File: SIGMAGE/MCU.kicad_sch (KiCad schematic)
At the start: 22 parts, among them U8 STM32F407VGTx, X1 STDCSU18M

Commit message: Finished schematic
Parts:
- added J10, J9: TSW10607GS, SIGMAGE:TSW10607GS, symbol SIGMAGE:TSW10607GS
- added J11, J12, J13: HTSW10807GD, SIGMAGE:HTSW10807GD, symbol SIGMAGE:HTSW10807GD
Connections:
- net ADC1_BYPAS: now also U8.93 (PB7)
- net ADC1_PDWN: now also U8.92 (PB6)
- net ADC2_BYPAS: now also U8.96 (PB9)
- net ADC2_DOUT: now also U8.91 (PB5); no longer U8.80 (PC12)
- net ADC2_LRCK: now also U8.29 (PA4); no longer U8.77 (PA15)
- net ADC2_PDWN: now also U8.95 (PB8)
- net GND: now also J10.6, J9.6
- net at U8.1 (PE2): now also J11.3
- net at U8.15 (PC0): now also J13.9
- net PHY_MDC: now reaches U8.16 (PC1)
- net at U8.17 (PC2): now also J13.10
- net at U8.18 (PC3): now also J13.11
- net at U8.2 (PE3): now also J11.4
- net at U8.23 (PA0): now also J13.1
- net PHY_REFCLK: now reaches U8.24 (PA1)
- net PHY_MDIO: now reaches U8.25 (PA2)
- net at U8.26 (PA3): now also J13.2
- net at U8.3 (PE4): now also J11.5
- net at U8.30 (PA5): now also J13.3
- net at U8.31 (PA6): now also J13.4
- net PHY_CRS_DV: now reaches U8.32 (PA7)
- net PHY_RXD0: now reaches U8.33 (PC4)
- net PHY_RXD1: now reaches U8.34 (PC5)
- net at U8.35 (PB0): now also J13.5
- net at U8.36 (PB1): now also J13.6
- net at U8.37 (PB2): now also J13.7
- net at U8.38 (PE7): now also J11.8
- net at U8.39 (PE8): now also J11.9
- net at U8.4 (PE5): now also J11.6
- net at U8.40 (PE9): now also J11.10
- net at U8.41 (PE10): now also J11.11
- net at U8.42 (PE11): now also J11.12
- net at U8.43 (PE12): now also J11.13
- net at U8.44 (PE13): now also J11.14
- net at U8.45 (PE14): now also J11.15
- net at U8.46 (PE15): now also J11.16
- net PHY_NRST: now reaches U8.47 (PB10)
- net PHY_TXEN: now reaches U8.48 (PB11)
- net at U8.5 (PE6): now also J11.7
- net at U8.53 (PB14): now also J13.8
- net at U8.55 (PD8): now also J12.9
- net at U8.56 (PD9): now also J12.10
- net at U8.57 (PD10): now also J12.11
- net at U8.58 (PD11): now also J12.12
- net at U8.59 (PD12): now also J12.13
- net at U8.60 (PD13): now also J12.14
- net at U8.61 (PD14): now also J12.15
- net at U8.62 (PD15): now also J12.16
- net at U8.65 (PC8): now also J13.12
- net at U8.66 (PC9): now also J13.13
- net USART1_CK: now reaches U8.67 (PA8)
- net USART1_CK: now also J9.5
- net USART1_TX: now reaches U8.68 (PA9)
- net USART1_TX: now also J9.3
- net USART1_RX: now reaches U8.69 (PA10)
- net USART1_RX: now also J9.4
- net PHY_TXD1: now reaches U8.7 (PC13)
- net USART1_CTS: now reaches U8.70 (PA11)
- net USART1_CTS: now also J9.1
- net USART1_RTS: now reaches U8.71 (PA12)
- net USART1_RTS: now also J9.2
- net JTMS_SWDIO: now reaches U8.72 (PA13)
- net JTMS_SWDIO: now also J10.1
- net JTCK_SWCLK: now reaches U8.76 (PA14)
- net JTCK_SWCLK: now also J10.2
- net at U8.79 (PC11): now also J13.14
- net at U8.8 (PC14): now also J13.15
- net at U8.81 (PD0): now also J12.1
- net at U8.82 (PD1): now also J12.2
- net at U8.83 (PD2): now also J12.3
- net at U8.84 (PD3): now also J12.4
- net at U8.85 (PD4): now also J12.5
- net at U8.86 (PD5): now also J12.6
- net at U8.87 (PD6): now also J12.7
- net at U8.88 (PD7): now also J12.8
- net JTDO_SWO: now reaches U8.89 (PB3)
- net JTDO_SWO: now also J10.4
- net at U8.9 (PC15): now also J13.16
- net JTRST: now reaches U8.90 (PB4)
- net JTRST: now also J10.5
- net at U8.97 (PE0): now also J11.1
- net at U8.98 (PE1): now also J11.2
- new net JTDI: J10.3, U8.77 (PA15)
- new net PHY_TXD0: U8.80 (PC12)
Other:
- moved on the sheet: C28, C29, C30, C31, C32, C33, C34, C35, C36, C37, C38, C39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

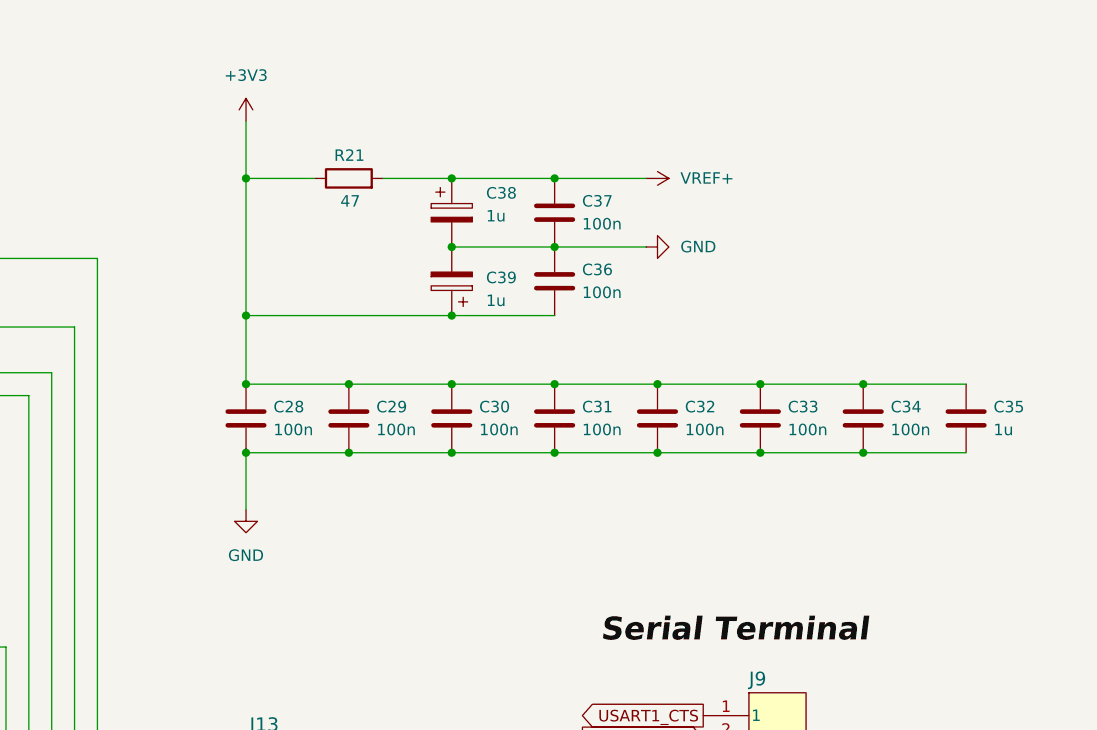
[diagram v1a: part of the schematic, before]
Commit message: Added PCB layout and started routing
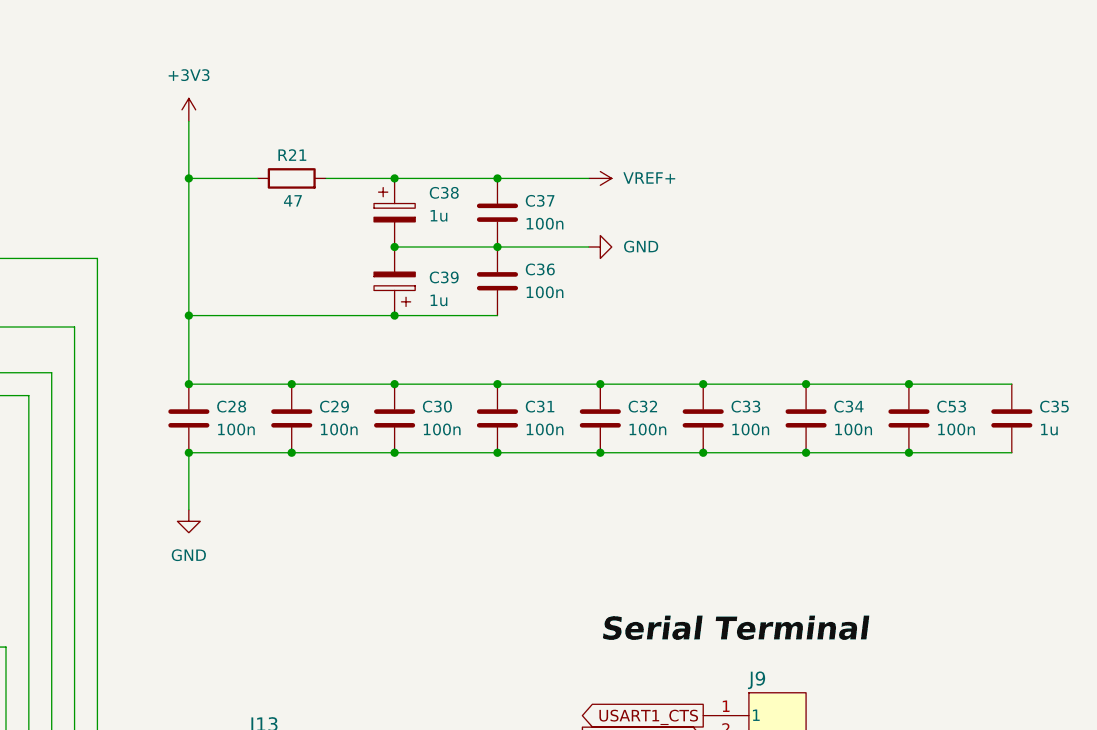
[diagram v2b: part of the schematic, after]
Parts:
- added C53: 100n, Capacitor_SMD:C_0603_1608Metric, symbol Device:C
- C28, C29, C30, C31, C32, C33, C34, C35, C36, C37, C38, C39, C40, C41, C42, C43, C44: footprint (none) -> Capacitor_SMD:C_0603_1608Metric
- R21, R22, R23: footprint (none) -> Resistor_SMD:R_0603_1608Metric
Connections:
- net +3V3: now also C53.1
- net GND: now also C53.2
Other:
- moved on the sheet: C28, C29, C30, C31, C32, C33, C34, C35, C36, C37, C38, C39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

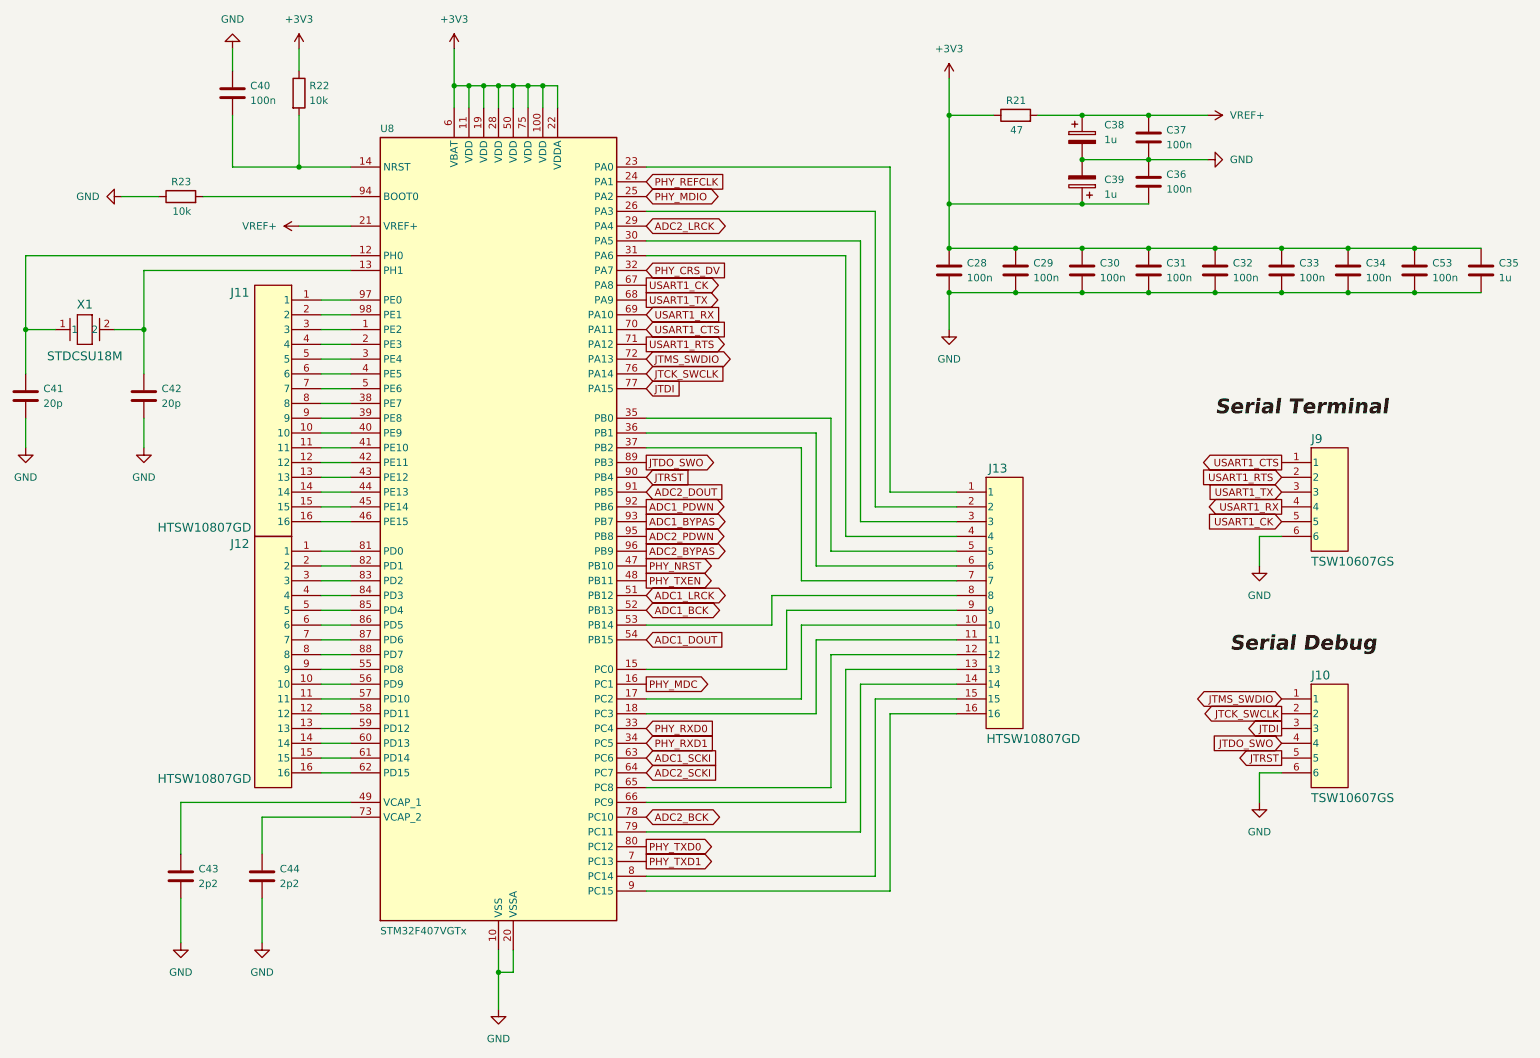
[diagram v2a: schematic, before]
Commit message: Almost finished routing
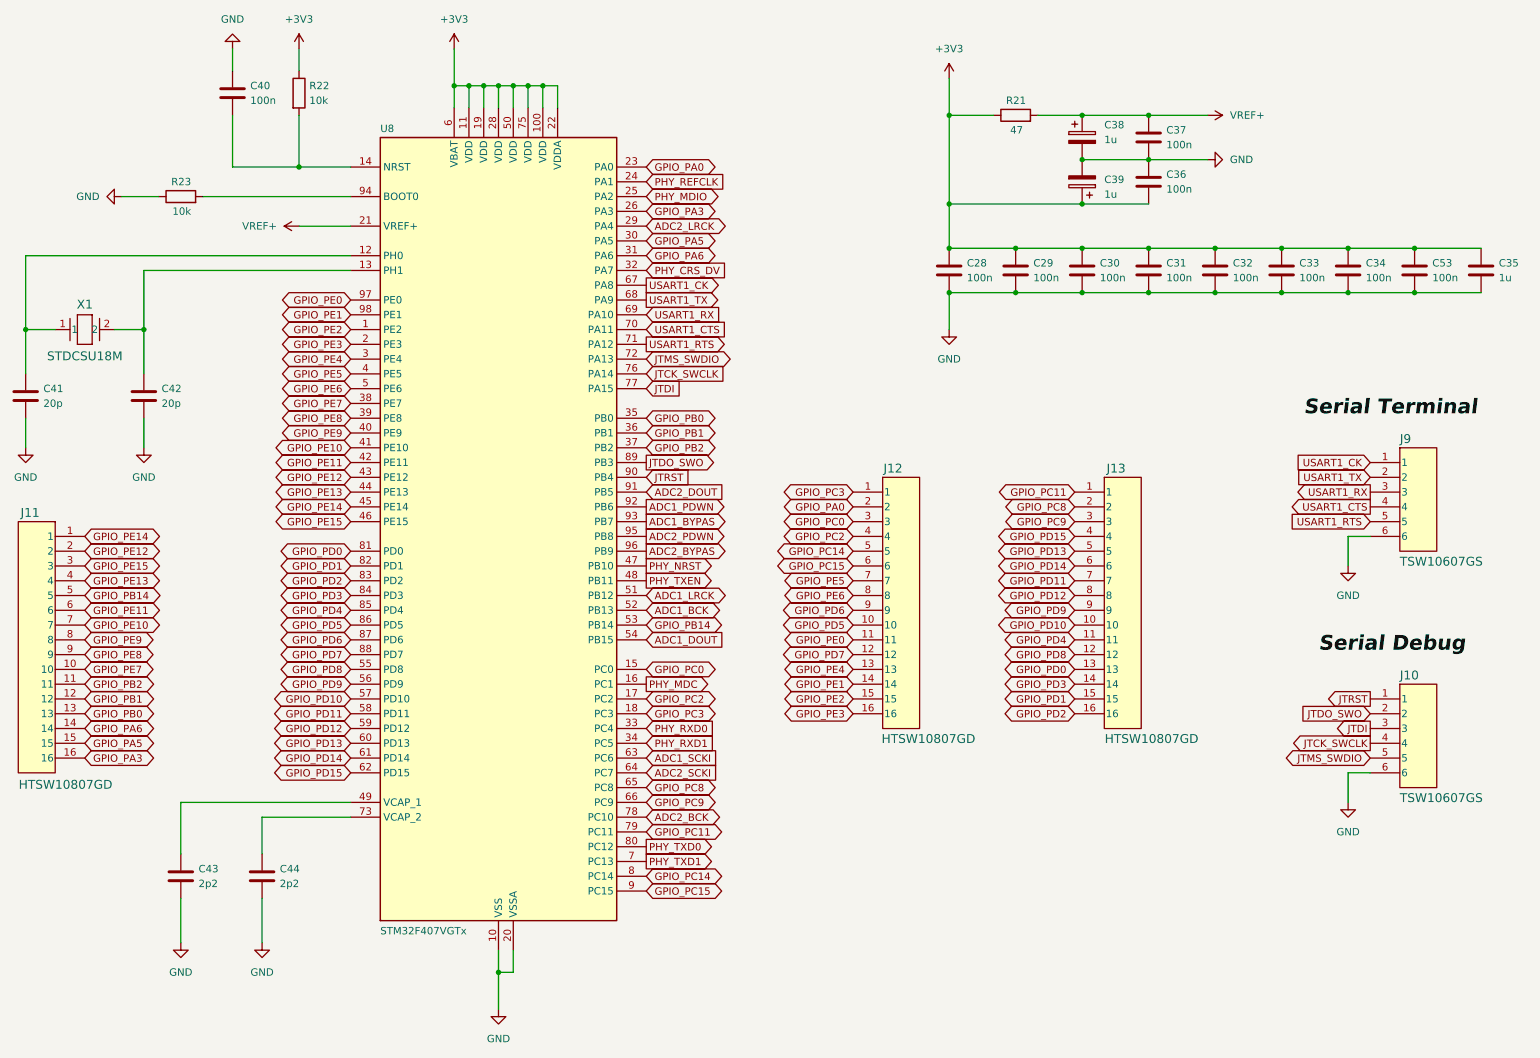
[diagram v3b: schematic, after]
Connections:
- net JTCK_SWCLK: now also J10.4; no longer J10.2
- net JTDO_SWO: now also J10.2; no longer J10.4
- net JTMS_SWDIO: now also J10.5; no longer J10.1
- net JTRST: now also J10.1; no longer J10.5
- net USART1_CK: now also J9.1; no longer J9.5
- net USART1_CTS: now also J9.4; no longer J9.1
- net USART1_RTS: now also J9.5; no longer J9.2
- net USART1_RX: now also J9.3; no longer J9.4
- net USART1_TX: now also J9.2; no longer J9.3
- net GPIO_PE15: now reaches J11.3
- net GPIO_PE15: now also U8.46 (PE15); no longer U8.1 (PE2)
- net GPIO_PC0: now reaches U8.15 (PC0)
- net GPIO_PC0: now also J12.3; no longer J13.9
- net GPIO_PC2: now reaches U8.17 (PC2)
- net GPIO_PC2: now also J12.4; no longer J13.10
- net GPIO_PC3: now reaches U8.18 (PC3)
- net GPIO_PC3: now also J12.1; no longer J13.11
- net GPIO_PE13: now reaches J11.4
- net GPIO_PE13: now also U8.44 (PE13); no longer U8.2 (PE3)
- net GPIO_PA0: now reaches U8.23 (PA0)
- net GPIO_PA0: now also J12.2; no longer J13.1
- net GPIO_PA3: now reaches U8.26 (PA3)
- net GPIO_PA3: now also J11.16; no longer J13.2
- net GPIO_PB14: now reaches J11.5
- net GPIO_PB14: now also U8.53 (PB14); no longer U8.3 (PE4)
- net GPIO_PA5: now reaches U8.30 (PA5)
- net GPIO_PA5: now also J11.15; no longer J13.3
- net GPIO_PA6: now reaches U8.31 (PA6)
- net GPIO_PA6: now also J11.14; no longer J13.4
- net GPIO_PB0: now reaches U8.35 (PB0)
- net GPIO_PB0: now also J11.13; no longer J13.5
- net GPIO_PB1: now reaches U8.36 (PB1)
- net GPIO_PB1: now also J11.12; no longer J13.6
- net GPIO_PB2: now reaches U8.37 (PB2)
- net GPIO_PB2: now also J11.11; no longer J13.7
- net GPIO_PE7: now reaches U8.38 (PE7)
- net GPIO_PE7: now also J11.10; no longer J11.8
- net GPIO_PE8: now reaches J11.9, U8.39 (PE8)
- net GPIO_PE11: now reaches J11.6
- net GPIO_PE11: now also U8.42 (PE11); no longer U8.4 (PE5)
- net GPIO_PE9: now reaches U8.40 (PE9)
- net GPIO_PE9: now also J11.8; no longer J11.10
- net GPIO_PE10: now reaches U8.41 (PE10)
- net GPIO_PE10: now also J11.7; no longer J11.11
- net GPIO_PE12: now reaches U8.43 (PE12)
- net GPIO_PE12: now also J11.2; no longer J11.13
- net GPIO_PE14: now reaches U8.45 (PE14)
- net GPIO_PE14: now also J11.1; no longer J11.15
- net GPIO_PE6: now reaches U8.5 (PE6)
- net GPIO_PE6: now also J12.8; no longer J11.7
- net GPIO_PD12: now reaches J13.8
- net GPIO_PD12: now also U8.59 (PD12); no longer U8.53 (PB14)
- net GPIO_PD6: now reaches J12.9
- net GPIO_PD6: now also U8.87 (PD6); no longer U8.55 (PD8)
- net GPIO_PD5: now reaches J12.10
- net GPIO_PD5: now also U8.86 (PD5); no longer U8.56 (PD9)
- net GPIO_PD10: now reaches U8.57 (PD10)
- net GPIO_PD10: now also J13.10; no longer J12.11
- net GPIO_PD11: now reaches U8.58 (PD11)
- net GPIO_PD11: now also J13.7; no longer J12.12
- net GPIO_PE4: now reaches J12.13
- net GPIO_PE4: now also U8.3 (PE4); no longer U8.59 (PD12)
- net GPIO_PD13: now reaches U8.60 (PD13)
- net GPIO_PD13: now also J13.5; no longer J12.14
- net GPIO_PD14: now reaches U8.61 (PD14)
- net GPIO_PD14: now also J13.6; no longer J12.15
- net GPIO_PD15: now reaches U8.62 (PD15)
- net GPIO_PD15: now also J13.4; no longer J12.16
- net GPIO_PC8: now reaches U8.65 (PC8)
- net GPIO_PC8: now also J13.2; no longer J13.12
- net GPIO_PC9: now reaches U8.66 (PC9)
- net GPIO_PC9: now also J13.3; no longer J13.13
- net GPIO_PC11: now reaches U8.79 (PC11)
- net GPIO_PC11: now also J13.1; no longer J13.14
- net GPIO_PC14: now reaches U8.8 (PC14)
- net GPIO_PC14: now also J12.5; no longer J13.15
- net GPIO_PD0: now reaches U8.81 (PD0)
- net GPIO_PD0: now also J13.13; no longer J12.1
- net GPIO_PD1: now reaches U8.82 (PD1)
- net GPIO_PD1: now also J13.15; no longer J12.2
- net GPIO_PD2: now reaches U8.83 (PD2)
- net GPIO_PD2: now also J13.16; no longer J12.3
- net GPIO_PD3: now reaches U8.84 (PD3)
- net GPIO_PD3: now also J13.14; no longer J12.4
- net GPIO_PD4: now reaches U8.85 (PD4)
- net GPIO_PD4: now also J13.11; no longer J12.5
- net GPIO_PC15: now reaches J12.6
- net GPIO_PC15: now also U8.9 (PC15); no longer U8.86 (PD5)
- net GPIO_PE5: now reaches J12.7
- net GPIO_PE5: now also U8.4 (PE5); no longer U8.87 (PD6)
- net GPIO_PD7: now reaches U8.88 (PD7)
- net GPIO_PD7: now also J12.12; no longer J12.8
- net GPIO_PE0: now reaches U8.97 (PE0)
- net GPIO_PE0: now also J12.11; no longer J11.1
- net GPIO_PE1: now reaches U8.98 (PE1)
- net GPIO_PE1: now also J12.14; no longer J11.2
- new net GPIO_PD8: J13.12, U8.55 (PD8)
- new net GPIO_PD9: J13.9, U8.56 (PD9)
- new net GPIO_PE2: J12.15, U8.1 (PE2)
- new net GPIO_PE3: J12.16, U8.2 (PE3)
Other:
- moved on the sheet: J10, J11, J12, J13, J9
